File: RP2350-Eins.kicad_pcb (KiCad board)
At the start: 4 copper layers, 68.6 x 53.3 mm, 72 parts, among them J1 CONN_PWR, J10 CONN_USB, J2 CONN_ICSP, J3 CONN_A, J4 CONN_P, J5 CONN_X, J6 CONN_DBG, J7 CONN_JTAG, J8 CONN_D1, J9 CONN_D2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

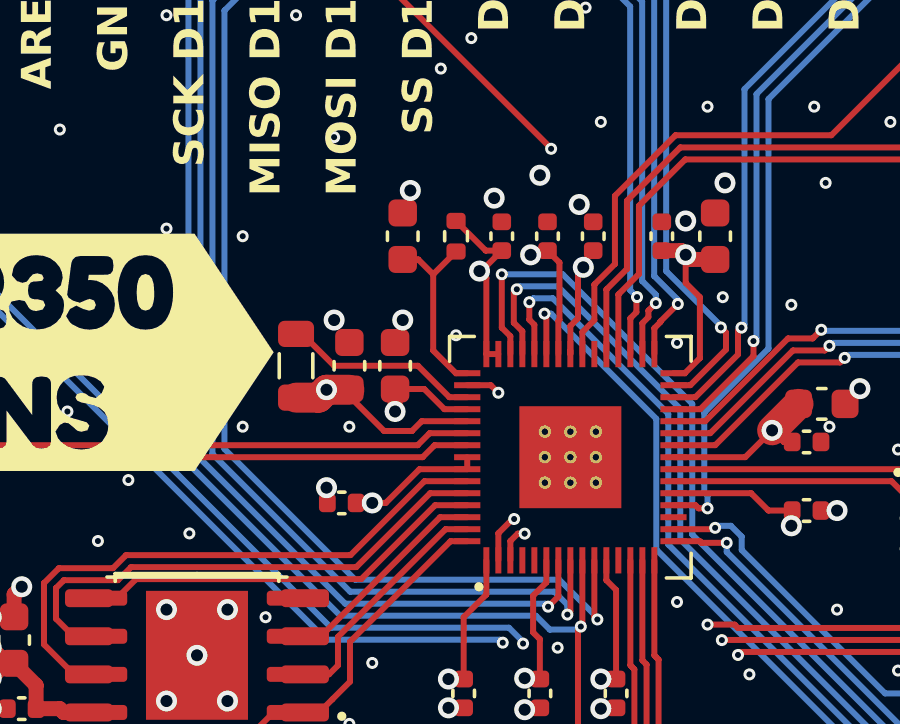
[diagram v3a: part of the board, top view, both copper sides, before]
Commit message: Moved staff around.
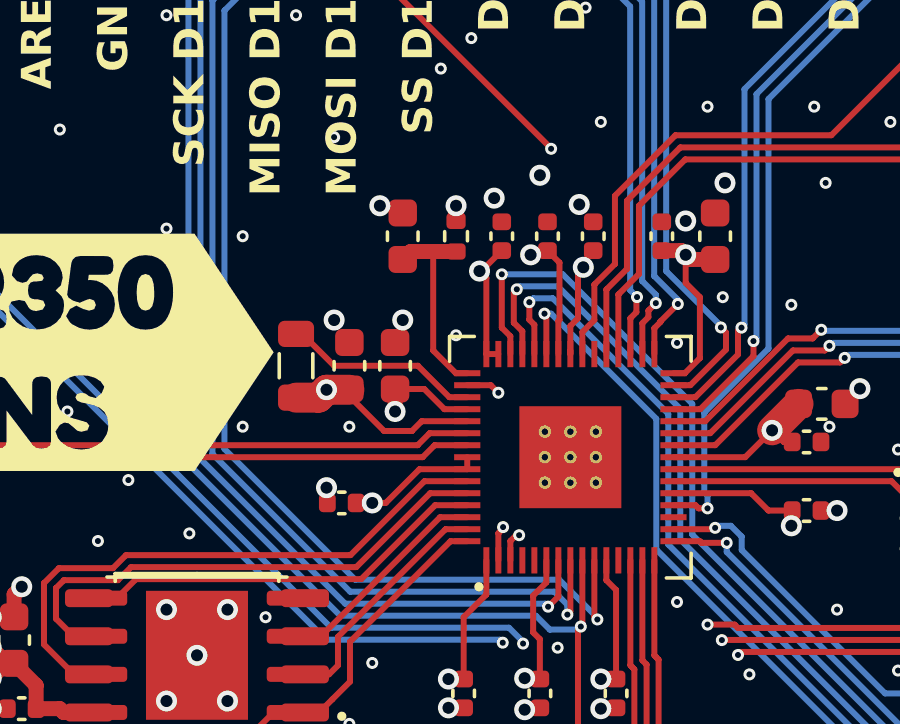
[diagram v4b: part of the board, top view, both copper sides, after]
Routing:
- net +3V3: track 57.0 -> 55.6 mm, vias 20 -> 21
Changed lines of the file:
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@@
 	)
 	(segment
+		(start 164.846 87.12)
+		(end 164.846 86.614)
+		(width 0.5)
+		(layer "F.Cu")
+		(net 1)
+	)
+	(segment
 		(start 151.638 103.378)
 		(end 150.848 103.378)
@@
 	)
 	(segment
-		(start 166.37 88.11)
-		(end 165.836 88.11)
-		(width 0.2)
-		(layer "F.Cu")
-		(net 1)
-	)
-	(segment
 		(start 165.2185 94.996)
 		(end 165.2185 95.396)
@@
 	)
 	(segment
-		(start 165.836 88.11)
-		(end 164.846 87.12)
-		(width 0.2)
-		(layer "F.Cu")
-		(net 1)
-	)
-	(segment
 		(start 172.974 91.694)
 		(end 172.472 92.196)
@@
 	)
 	(via
+		(at 164.846 86.614)
+		(size 0.7)
+		(drill 0.4)
+		(layers "F.Cu" "B.Cu")
+		(net 1)
+	)
+	(via
 		(at 180.594 103.378)
 		(size 0.4)
@@
 	)
 	(via
-		(at 163.322 86.106)
+		(at 162.306 86.614)
 		(size 0.7)
 		(drill 0.4)
@@
 	)
 	(segment
-		(start 166.902 97.544)
+		(start 166.849939 97.596061)
 		(end 166.656 97.79)
 		(width 0.2)
@@
 	)
 	(segment
-		(start 167.132 97.544)
-		(end 166.902 97.544)
+		(start 166.948953 97.596061)
+		(end 166.849939 97.596061)
 		(width 0.2)
 		(layer "F.Cu")
@@
 	)
 	(via
-		(at 167.132 97.544)
+		(at 166.948953 97.596061)
 		(size 0.4)
 		(drill 0.2)
@@
 	)
 	(segment
-		(start 167.132 97.544)
-		(end 171.188 97.544)
+		(start 176.398797 96.200889)
+		(end 179.997686 92.602)
+		(width 0.2)
+		(layer "In2.Cu")
+		(net 12)
+	)
+	(segment
+		(start 166.948953 97.596061)
+		(end 167.074556 97.470458)
 		(width 0.2)
 		(layer "In2.Cu")
@@
 	)
 	(segment
-		(start 171.188 97.544)
-		(end 172.531111 96.200889)
+		(start 172.531111 96.200889)
+		(end 176.398797 96.200889)
 		(width 0.2)
 		(layer "In2.Cu")
@@
 	)
 	(segment
-		(start 176.398797 96.200889)
-		(end 179.997686 92.602)
+		(start 182.8332 92.602)
+		(end 184.7076 90.7276)
 		(width 0.2)
 		(layer "In2.Cu")
@@
 	)
 	(segment
-		(start 179.997686 92.602)
-		(end 182.8332 92.602)
+		(start 167.074556 97.470458)
+		(end 171.261542 97.470458)
 		(width 0.2)
 		(layer "In2.Cu")
@@
 	)
 	(segment
-		(start 172.531111 96.200889)
-		(end 176.398797 96.200889)
+		(start 179.997686 92.602)
+		(end 182.8332 92.602)
 		(width 0.2)
 		(layer "In2.Cu")
@@
 	)
 	(segment
-		(start 182.8332 92.602)
-		(end 184.7076 90.7276)
+		(start 171.261542 97.470458)
+		(end 172.531111 96.200889)
 		(width 0.2)
 		(layer "In2.Cu")
@@
 	)
 	(segment
-		(start 166.729946 97.056369)
-		(end 166.256 97.530315)
+		(start 166.413446 97.325446)
+		(end 166.413446 97.372869)
 		(width 0.2)
 		(layer "F.Cu")
@@
 	)
 	(segment
-		(start 166.782406 97.056369)
-		(end 166.729946 97.056369)
+		(start 166.413446 97.372869)
+		(end 166.256 97.530315)
 		(width 0.2)
 		(layer "F.Cu")
@@
 	)
 	(via
-		(at 166.782406 97.056369)
+		(at 166.413446 97.325446)
 		(size 0.4)
 		(drill 0.2)
@@
 	)
 	(segment
-		(start 166.794775 97.044)
-		(end 167.339107 97.044)
-		(width 0.2)
-		(layer "In2.Cu")
-		(net 13)
-	)
-	(segment
-		(start 171.022314 97.144)
-		(end 172.365425 95.800889)
-		(width 0.2)
-		(layer "In2.Cu")
-		(net 13)
-	)
-	(segment
-		(start 166.782406 97.056369)
-		(end 166.794775 97.044)
+		(start 166.668434 97.070458)
+		(end 171.095856 97.070458)
 		(width 0.2)
 		(layer "In2.Cu")
@@
 	)
 	(segment
-		(start 184.07016 90.700154)
-		(end 184.07016 90.55944)
+		(start 166.413446 97.325446)
+		(end 166.668434 97.070458)
 		(width 0.2)
 		(layer "In2.Cu")
@@
 	)
 	(segment
-		(start 167.439107 97.144)
-		(end 171.022314 97.144)
+		(start 184.07016 90.700154)
+		(end 184.07016 90.55944)
 		(width 0.2)
 		(layer "In2.Cu")
@@
 	)
 	(segment
-		(start 167.339107 97.044)
-		(end 167.439107 97.144)
+		(start 176.233111 95.800889)
+		(end 179.832 92.202)
 		(width 0.2)
 		(layer "In2.Cu")
@@
 	)
 	(segment
-		(start 176.233111 95.800889)
-		(end 179.832 92.202)
+		(start 171.095856 97.070458)
+		(end 172.365425 95.800889)
 		(width 0.2)
 		(layer "In2.Cu")
@@
 	)
 	(segment
-		(start 164.846 88.14)
-		(end 164.084 88.902)
-		(width 0.2)
-		(layer "F.Cu")
-		(net 72)
-	)
-	(segment
-		(start 164.84 92.196)
-		(end 165.2185 92.196)
-		(width 0.2)
-		(layer "F.Cu")
-		(net 72)
-	)
-	(segment
-		(start 163.068 88.405)
-		(end 163.587 88.405)
-		(width 0.2)
+		(start 163.333 88.14)
+		(end 163.068 88.405)
+		(width 0.5)
 		(layer "F.Cu")
 		(net 72)
 	)
 	(segment
-		(start 164.084 88.902)
-		(end 164.084 91.44)
+		(start 164.084 91.44)
+		(end 164.84 92.196)
 		(width 0.2)
 		(layer "F.Cu")
@@
 	)
 	(segment
-		(start 163.587 88.405)
-		(end 164.084 88.902)
-		(width 0.2)
+		(start 164.846 88.14)
+		(end 163.333 88.14)
+		(width 0.5)
 		(layer "F.Cu")
 		(net 72)
 	)
 	(segment
-		(start 164.844 88.138)
-		(end 164.846 88.14)
+		(start 164.84 92.196)
+		(end 165.2185 92.196)
 		(width 0.2)
 		(layer "F.Cu")
@@
 	)
 	(segment
-		(start 164.084 91.44)
-		(end 164.84 92.196)
+		(start 164.084 88.14)
+		(end 164.084 91.44)
 		(width 0.2)
 		(layer "F.Cu")
